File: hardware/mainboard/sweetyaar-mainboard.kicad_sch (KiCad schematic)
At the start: 107 parts, among them Q1 MMBT3904

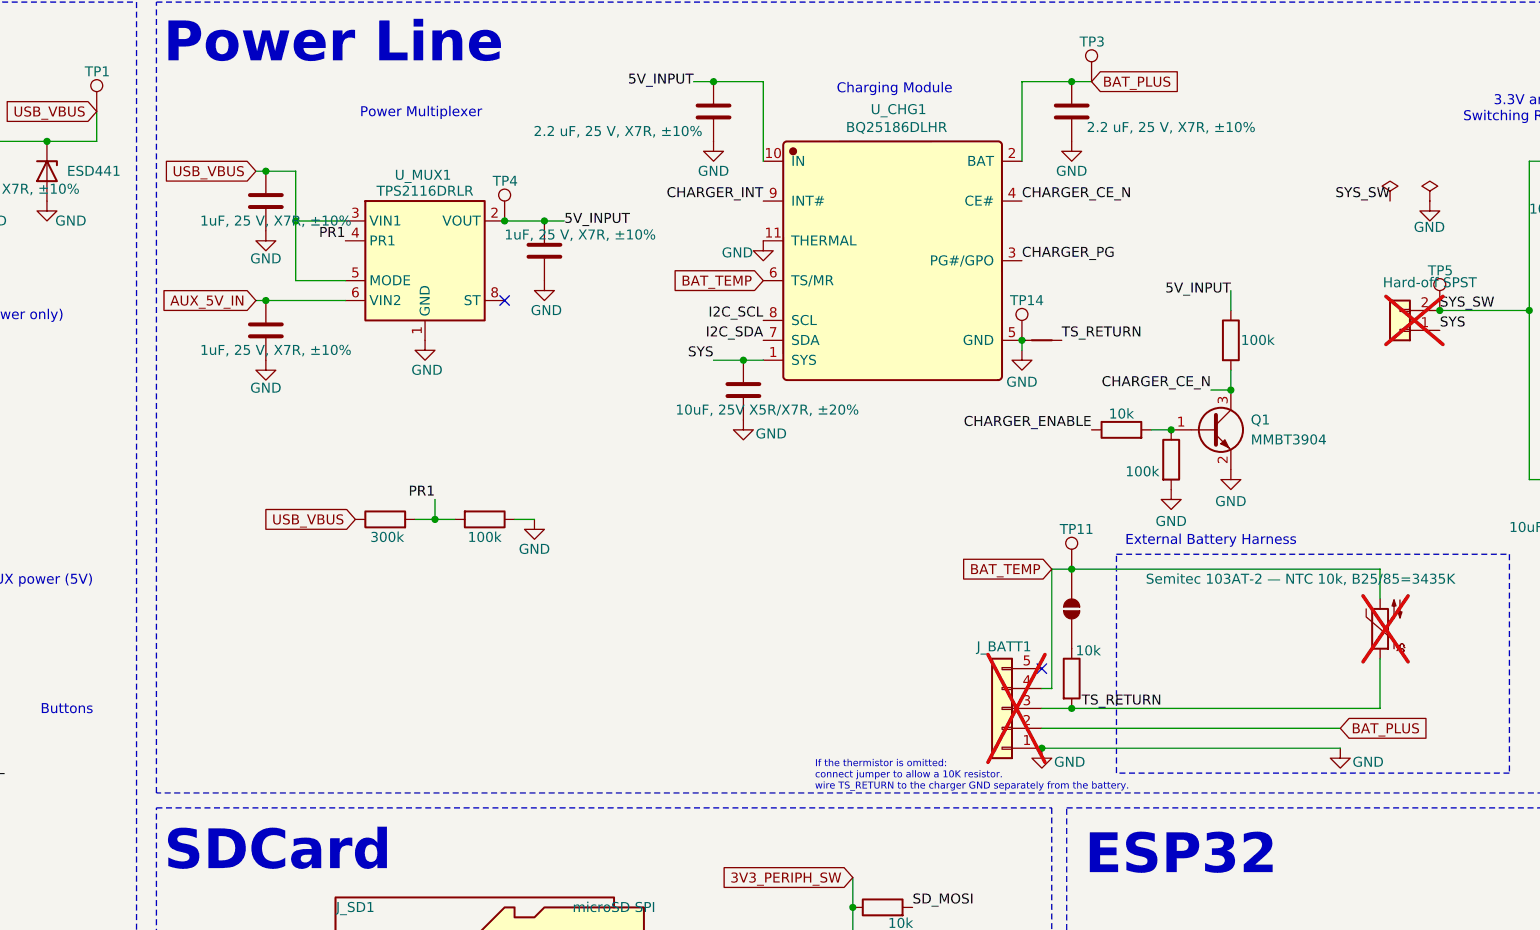
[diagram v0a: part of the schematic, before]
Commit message: Changing power mux to TPS2121 (higher allowed voltage to deal with spikes and uncontrolled AUX)
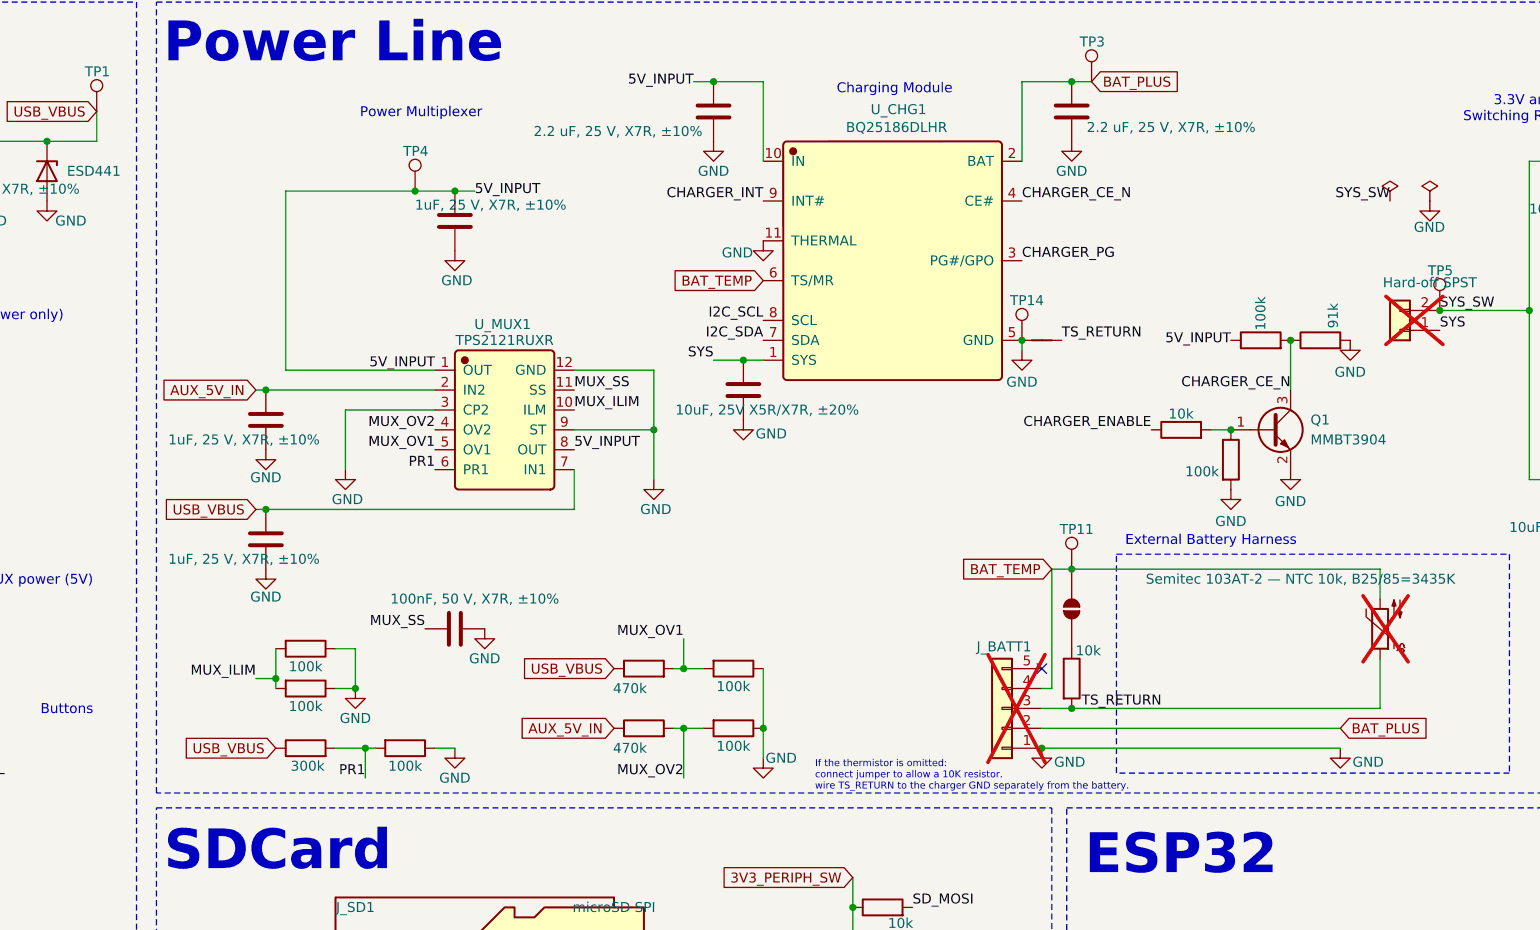
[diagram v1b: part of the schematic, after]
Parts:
- added C_MUX_SS1: 100nF, 50 V, X7R, ±10%, Capacitor_SMD:C_0603_1608Metric, symbol Device:C
- added R_CHARGER_CE_DIV2: 91k, Resistor_SMD:R_0603_1608Metric, symbol Device:R
- added R_MUX_ILIM1, R_MUX_ILIM2, R_MUX_OV_DIV2, R_MUX_OV_DIV4: 100k, Resistor_SMD:R_0603_1608Metric, symbol Device:R
- added R_MUX_OV_DIV1, R_MUX_OV_DIV3: 470k, Resistor_SMD:R_0603_1608Metric, symbol Device:R
- U_MUX1: value TPS2116DRLR -> TPS2121RUXR; footprint SweetYaar:SOT-583-8 - C3235557 -> Package_DFN_QFN:Texas_VQFN-HR-12_2x2.5mm_P0.5mm; symbol Power_Management:TPS2116DRL -> SweetYaar:TPS2121RUXR; LCSC C3235557 -> C485916; Manufacturer (none) -> Texas Instruments; Manufacturer Part (none) -> TPS2121RUXR
- renumbered R_CHARGER_CE_PU1 to R_CHARGER_CE_DIV1
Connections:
- net 5V_INPUT: now also U_MUX1.1 (OUT), U_MUX1.8 (OUT); no longer U_MUX1.2 (VOUT), U_MUX1.7 (VOUT)
- net AUX_5V_IN: now also U_MUX1.2 (IN2), R_MUX_OV_DIV3.1; no longer U_MUX1.6 (VIN2)
- net CHARGER_CE_N: now also R_CHARGER_CE_DIV2.1
- net GND: now also U_MUX1.12 (GND), U_MUX1.3 (CP2), U_MUX1.9 (ST), C_MUX_SS1.1, R_CHARGER_CE_DIV2.2, R_MUX_ILIM1.1, R_MUX_ILIM2.1, R_MUX_OV_DIV2.1, R_MUX_OV_DIV4.1; no longer U_MUX1.1 (GND)
- net PR1: now also U_MUX1.6 (PR1); no longer U_MUX1.4 (PR1)
- net USB_VBUS: now also U_MUX1.7 (IN1), R_MUX_OV_DIV1.1; no longer U_MUX1.3 (VIN1), U_MUX1.5 (MODE)
- new net MUX_ILIM: R_MUX_ILIM1.2, R_MUX_ILIM2.2, U_MUX1.10 (ILM)
- new net MUX_OV1: R_MUX_OV_DIV1.2, R_MUX_OV_DIV2.2, U_MUX1.5 (OV1)
- new net MUX_OV2: R_MUX_OV_DIV3.2, R_MUX_OV_DIV4.2, U_MUX1.4 (OV2)
- new net MUX_SS: C_MUX_SS1.2, U_MUX1.11 (SS)
- no-connect marks 16 -> 15
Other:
- moved on the sheet: Q1, TP4

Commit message: removing diode on AUX power; silkscreen changes
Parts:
- removed D2: ESD441, SweetYaar:Texas_DPY0002A_0.6x1mm_P0.65mm, symbol Device:D_Zener
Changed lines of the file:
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@@
 	)
 	(junction
-		(at 54.61 124.46)
-		(diameter 0)
-		(color 0 0 0 0)
-	)
-	(junction
 		(at 54.61 116.84)
 		(diameter 0)
@@
 					(unit 1)
 				)
-			)
-		)
-	)
-	(symbol
-		(lib_id "Device:D_Zener")
-		(at 54.61 120.65 270)
-		(unit 1)
-		(body_style 1)
-		(exclude_from_sim no)
-		(in_bom yes)
-		(on_board yes)
-		(in_pos_files yes)
-		(dnp no)
-		(fields_autoplaced yes)
-		(property "Reference" "D2"
-			(at 52.07 121.9201 90)
-			(hide yes)
-			(show_name no)
-			(do_not_autoplace no)
-			(effects
-				(font
-					(size 1.27 1.27)
-				)
-				(justify right)
-			)
-		)
-		(property "Value" "ESD441"
-			(at 57.15 120.6499 90)
-			(show_name no)
-			(do_not_autoplace no)
-			(effects
-				(font
-					(size 1.27 1.27)
-				)
-				(justify left)
-			)
-		)
-		(property "Footprint" "SweetYaar:Texas_DPY0002A_0.6x1mm_P0.65mm"
-			(at 54.61 120.65 0)
-			(hide yes)
-			(show_name no)
-			(do_not_autoplace no)
-			(effects
-				(font
-					(size 1.27 1.27)
-				)
-			)
-		)
-		(property "Datasheet" ""
-			(at 54.61 120.65 0)
-			(hide yes)
-			(show_name no)
-			(do_not_autoplace no)
-			(effects
-				(font
-					(size 1.27 1.27)
-				)
-			)
-		)
-		(property "Description" "Zener diode"
-			(at 54.61 120.65 0)
-			(hide yes)
-			(show_name no)
-			(do_not_autoplace no)
-			(effects
-				(font
-					(size 1.27 1.27)
-				)
-			)
-		)
-		(property "LCSC" "C53161160"
-			(at 54.61 120.65 270)
-			(hide yes)
-			(show_name no)
-			(do_not_autoplace no)
-			(effects
-				(font
-					(size 1.27 1.27)
-				)
-			)
-		)
-		(property "FT Rotation Offset" ""
-			(at 54.61 120.65 90)
-			(hide yes)
-			(show_name no)
-			(do_not_autoplace no)
-			(effects
-				(font
-					(size 1.27 1.27)
-				)
-			)
-		)
-		(property "Sim.Device" ""
-			(at 54.61 120.65 90)
-			(hide yes)
-			(show_name no)
-			(do_not_autoplace no)
-			(effects
-				(font
-					(size 1.27 1.27)
-				)
-			)
-		)
-		(property "Sim.Pins" ""
-			(at 54.61 120.65 90)
-			(hide yes)
-			(show_name no)
-			(do_not_autoplace no)
-			(effects
-				(font
-					(size 1.27 1.27)
-				)
-			)
-		)
-		(pin "2"
-		)
-		(pin "1"
-		)
-		(instances
-			(project "sweetyaar-mainboard"
-				(path "/a2bc0001-0000-4000-8000-000000000001"
-					(reference "D2")
-					(unit 1)
-				)

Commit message: Creating production v1.0 manufacturing files
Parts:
- C_3V3_OUT1, C_5V_OUT1, C_5V_OUT2: value 22uF, 16 V, X5R/X7R, ±20% -> 22uF, 25 V, X5R, ±10%; LCSC C90146 -> C12891
- C_BAT_SW_IN1, C_ESP_EN1, C_MUX1, C_MUX2, C_MUX4, C_SD_SW_IN1: value 1uF, 25 V, X7R, ±10% -> 1uF, 50 V, X5R, ±10%; LCSC C29936 -> C15849
- C_CHG_BAT1, C_MUX3: value 2.2 uF, 25 V, X7R, ±10% -> 4.7 uF, 25 V, X5R, ±10%; LCSC C126591 -> C1779
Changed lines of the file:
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@@
 			)
 		)
-		(property "Value" "1uF, 25 V, X7R, ±10%"
+		(property "Value" "1uF, 50 V, X5R, ±10%"
 			(at 143.002 70.358 0)
 			(show_name no)
@@
 			)
 		)
-		(property "Datasheet" ""
+		(property "Datasheet" "https://www.lcsc.com/datasheet/C15849.pdf"
 			(at 138.43 72.39 0)
 			(hide yes)
@@
 			)
 		)
-		(property "LCSC" "C29936"
+		(property "LCSC" "C15849"
 			(at 138.43 72.39 0)
 			(hide yes)
@@
 			)
 		)
-		(property "Value" "1uF, 25 V, X7R, ±10%"
+		(property "Value" "1uF, 50 V, X5R, ±10%"
 			(at 111.506 115.57 0)
 			(show_name no)
@@
 			)
 		)
-		(property "Datasheet" ""
+		(property "Datasheet" "https://www.lcsc.com/datasheet/C15849.pdf"
 			(at 114.3 113.03 0)
 			(hide yes)
@@
 			)
 		)
-		(property "LCSC" "C29936"
+		(property "LCSC" "C15849"
 			(at 114.3 113.03 0)
 			(hide yes)
@@
 			)
 		)
-		(property "Value" "1uF, 25 V, X7R, ±10%"
+		(property "Value" "1uF, 50 V, X5R, ±10%"
 			(at 111.506 100.33 0)
 			(show_name no)
@@
 			)
 		)
-		(property "Datasheet" ""
+		(property "Datasheet" "https://www.lcsc.com/datasheet/C15849.pdf"
 			(at 114.3 97.79 0)
 			(hide yes)
@@
 			)
 		)
-		(property "LCSC" "C29936"
+		(property "LCSC" "C15849"
 			(at 114.3 97.79 0)
 			(hide yes)
@@
 			)
 		)
-		(property "Value" "2.2 uF, 25 V, X7R, ±10%"
+		(property "Value" "4.7 uF, 25 V, X5R, ±10%"
 			(at 159.258 60.96 0)
 			(show_name no)
@@
 			)
 		)
-		(property "Datasheet" ""
+		(property "Datasheet" "https://www.lcsc.com/datasheet/C1779.pdf"
 			(at 171.45 58.42 0)
 			(hide yes)
@@
 			)
 		)
-		(property "LCSC" "C126591"
+		(property "LCSC" "C1779"
 			(at 171.45 58.42 0)
 			(hide yes)
@@
 			)
 		)
-		(property "Value" "2.2 uF, 25 V, X7R, ±10%"
+		(property "Value" "4.7 uF, 25 V, X5R, ±10%"
 			(at 229.87 60.452 0)
 			(show_name no)
@@
 			)
 		)
-		(property "Datasheet" ""
+		(property "Datasheet" "https://www.lcsc.com/datasheet/C1779.pdf"
 			(at 217.17 58.42 0)
 			(hide yes)
@@
 			)
 		)
-		(property "LCSC" "C126591"
+		(property "LCSC" "C1779"
 			(at 217.17 58.42 0)
 			(hide yes)
@@
 			)
 		)
-		(property "Value" "22uF, 16 V, X5R/X7R, ±20%"
+		(property "Value" "22uF, 25 V, X5R, ±10%"
 			(at 339.09 70.866 0)
 			(show_name no)
@@
 			)
 		)
-		(property "Datasheet" ""
+		(property "Datasheet" "https://www.lcsc.com/datasheet/C12891.pdf"
 			(at 336.55 68.58 0)
 			(hide yes)
@@
 			)
 		)
-		(property "LCSC" "C90146"
+		(property "LCSC" "C12891"
 			(at 336.55 68.58 0)
 			(hide yes)
@@
 			)
 		)
-		(property "Value" "22uF, 16 V, X5R/X7R, ±20%"
+		(property "Value" "22uF, 25 V, X5R, ±10%"
 			(at 331.47 119.126 0)
 			(show_name no)
@@
 			)
 		)
-		(property "Datasheet" ""
+		(property "Datasheet" "https://www.lcsc.com/datasheet/C12891.pdf"
 			(at 334.01 116.84 0)
 			(hide yes)
@@
 			)
 		)
-		(property "LCSC" "C90146"
+		(property "LCSC" "C12891"
 			(at 334.01 116.84 0)
 			(hide yes)
@@
 			)
 		)
-		(property "Value" "22uF, 16 V, X5R/X7R, ±20%"
+		(property "Value" "22uF, 25 V, X5R, ±10%"
 			(at 341.63 119.38 0)
 			(show_name no)
@@
 			)
 		)
-		(property "Datasheet" ""
+		(property "Datasheet" "https://www.lcsc.com/datasheet/C12891.pdf"
 			(at 339.09 116.84 0)
 			(hide yes)
@@
 			)
 		)
-		(property "LCSC" "C90146"
+		(property "LCSC" "C12891"
 			(at 339.09 116.84 0)
 			(hide yes)
@@
 			)
 		)
-		(property "Value" "1uF, 25 V, X7R, ±10%"
+		(property "Value" "1uF, 50 V, X5R, ±10%"
 			(at 312.42 200.66 0)
 			(show_name no)
@@
 			)
 		)
-		(property "Datasheet" ""
+		(property "Datasheet" "https://www.lcsc.com/datasheet/C15849.pdf"
 			(at 311.15 198.12 0)
 			(hide yes)
@@
 			)
 		)
-		(property "LCSC" "C29936"
+		(property "LCSC" "C15849"
 			(at 311.15 198.12 0)
 			(hide yes)
@@
 			)
 		)
-		(property "FT Rotation Offset" ""
-			(at 157.48 246.38 0)
-			(hide yes)
-			(show_name no)
-			(do_not_autoplace no)
-			(effects
-				(font
-					(size 1.27 1.27)
-				)
-			)
-		)
 		(property "Sim.Device" ""
 			(at 157.48 246.38 0)
@@
 			)
 		)
-		(property "Value" "1uF, 25 V, X7R, ±10%"
+		(property "Value" "1uF, 50 V, X5R, ±10%"
 			(at 365.76 81.28 0)
 			(show_name no)
@@
 			)
 		)
-		(property "Datasheet" ""
+		(property "Datasheet" "https://www.lcsc.com/datasheet/C15849.pdf"
 			(at 364.49 78.74 0)
 			(hide yes)
@@
 			)
 		)
-		(property "LCSC" "C29936"
+		(property "LCSC" "C15849"
 			(at 364.49 78.74 0)
 			(hide yes)
@@
 			)
 		)
-		(property "Value" "1uF, 25 V, X7R, ±10%"
+		(property "Value" "1uF, 50 V, X5R, ±10%"
 			(at 250.19 262.89 0)
 			(show_name no)
@@
 			)
 		)
-		(property "Datasheet" ""
+		(property "Datasheet" "https://www.lcsc.com/datasheet/C15849.pdf"
 			(at 248.92 260.35 0)
 			(hide yes)
@@
 			)
 		)
-		(property "LCSC" "C29936"
+		(property "LCSC" "C15849"
 			(at 248.92 260.35 0)
 			(hide yes)
